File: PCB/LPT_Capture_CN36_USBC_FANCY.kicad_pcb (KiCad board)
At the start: 2 copper layers, 68 x 31.7 mm, 26 parts, among them J1 GSB1C411101DS1HR, J2 112-036-213R001, Q1 SL2301S, Q2 SL2301S, U1 FT245RL

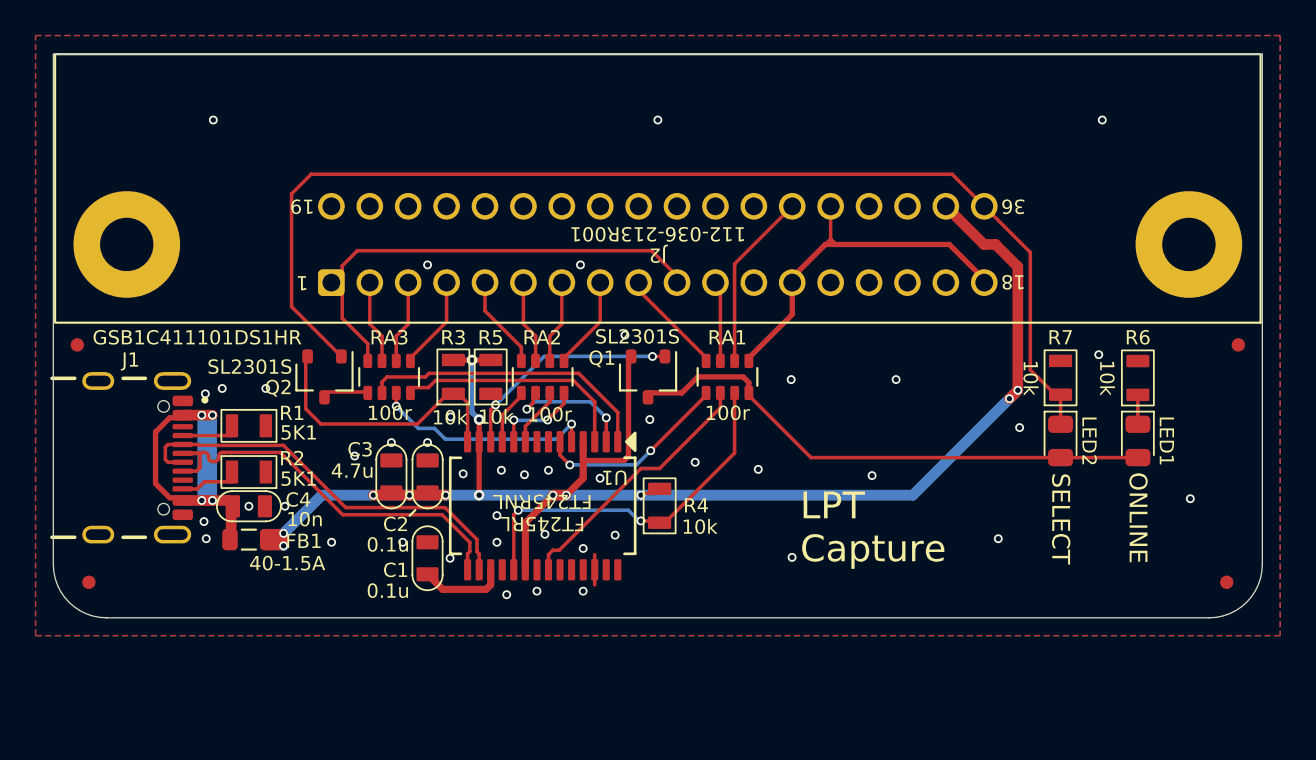
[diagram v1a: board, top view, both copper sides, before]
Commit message: cn36: board dims, leds, housing
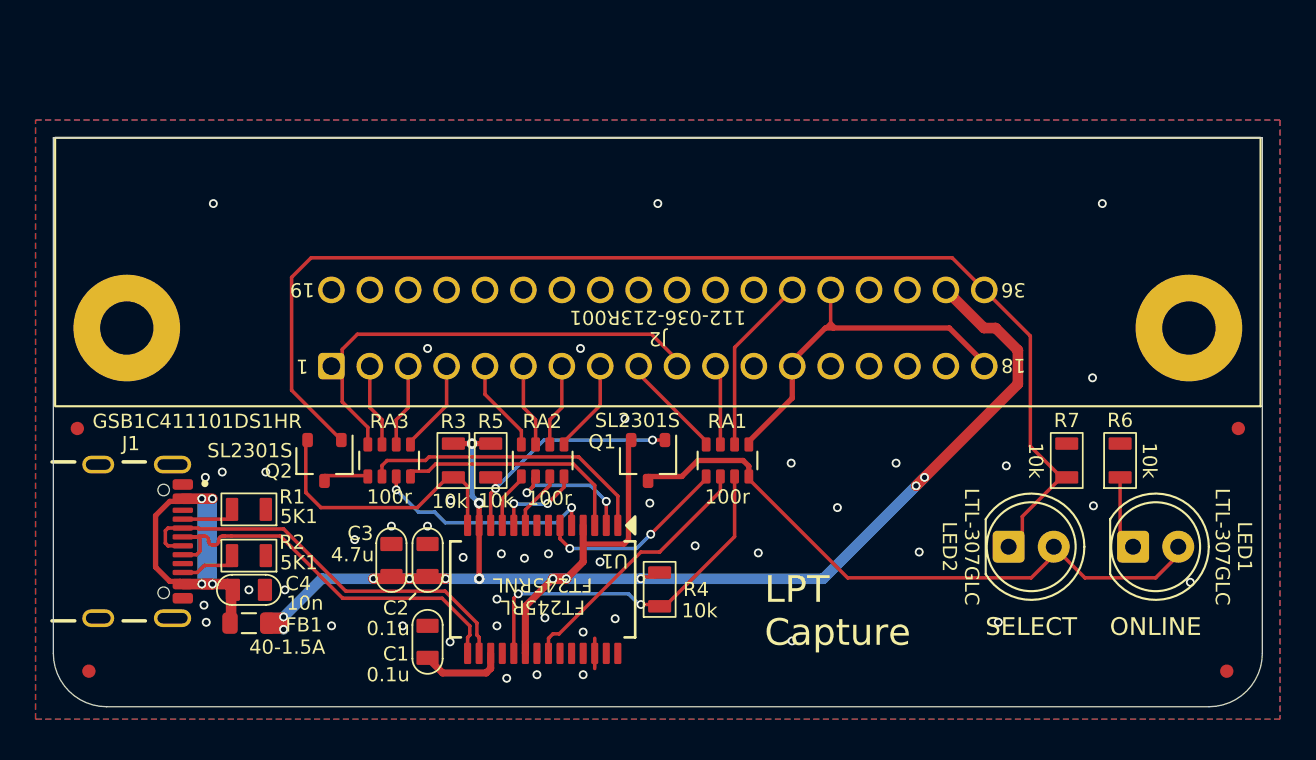
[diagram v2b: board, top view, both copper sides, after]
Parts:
- added N1: Housing, 000_LOCAL:Housing_CN36_shell_snap, F.Cu at (150.0, 100.0)
- LED1: value ONLINE -> LTL-307GLC; footprint 000_LOCAL:LED_0805 -> 000_LOCAL:LED_D5.0mm
- LED2: value SELECT -> LTL-307GLC; footprint 000_LOCAL:LED_0805 -> 000_LOCAL:LED_D5.0mm
- moved LED2 6.17 mm to (171.0, 107.0), turned to 0 degrees
- moved LED1 6.03 mm to (178.0, 107.0), turned to 0 degrees
- moved REF** 5.00 mm to (118.0, 114.0)
- moved REF** 5.00 mm to (182.0, 114.0)
- moved R6 4.75 mm to (176.0, 102.2)
- moved C2 4.70 mm to (137.1, 107.7)
- moved C3 4.70 mm to (135.0, 107.7)
- moved C4 4.70 mm to (127.0, 109.4)
- moved FB1 4.70 mm to (127.0, 111.3)
- moved J1 4.70 mm to (118.5, 106.7)
- moved J2 4.70 mm to (150.0, 94.7)
- moved Q1 4.70 mm to (149.4, 102.2)
- moved Q2 4.70 mm to (131.2, 102.2)
- moved R1 4.70 mm to (127.0, 104.9)
- moved R2 4.70 mm to (127.0, 107.5)
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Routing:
- net /ONLINE: track 30.5 -> 36.3 mm
- net /~{SELIN}: track 64.9 -> 68.7 mm
- net VCC: track 90.8 -> 87.9 mm
- net Net-(LED1-K): track 1.65 -> 4.20 mm
- net GND: vias 44 -> 46
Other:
- board size 68 x 31.7 mm -> 68 x 32 mm

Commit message: cn36 cover shape
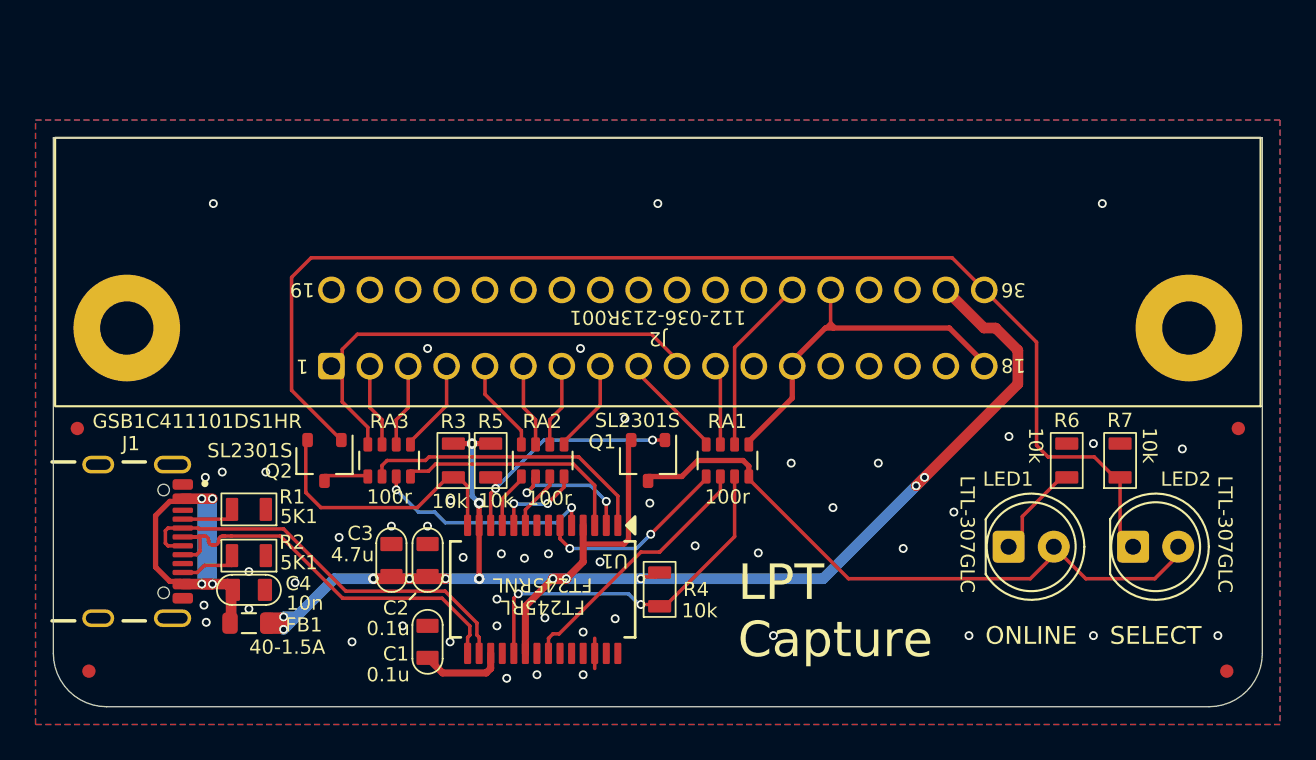
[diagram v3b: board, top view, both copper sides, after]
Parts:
- renumbered LED2 to LED1, LED1 to LED2, R7 to R6, R6 to R7
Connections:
- LED1 pad 1: /~{SELIN} -> Net-(LED1-K)
- LED2 pad 1: Net-(LED1-K) -> /~{SELIN}
- R6 pad 1: /~{SELIN} -> Net-(LED1-K)
- R7 pad 1: Net-(LED1-K) -> /~{SELIN}
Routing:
- net /~{SELIN}: track 68.7 -> 70.3 mm
- net Net-(LED1-K): track 4.20 -> 5.43 mm
- net GND: vias 46 -> 49

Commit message: cn36: missing datasheet, add RA4, refactor parts of cover scad
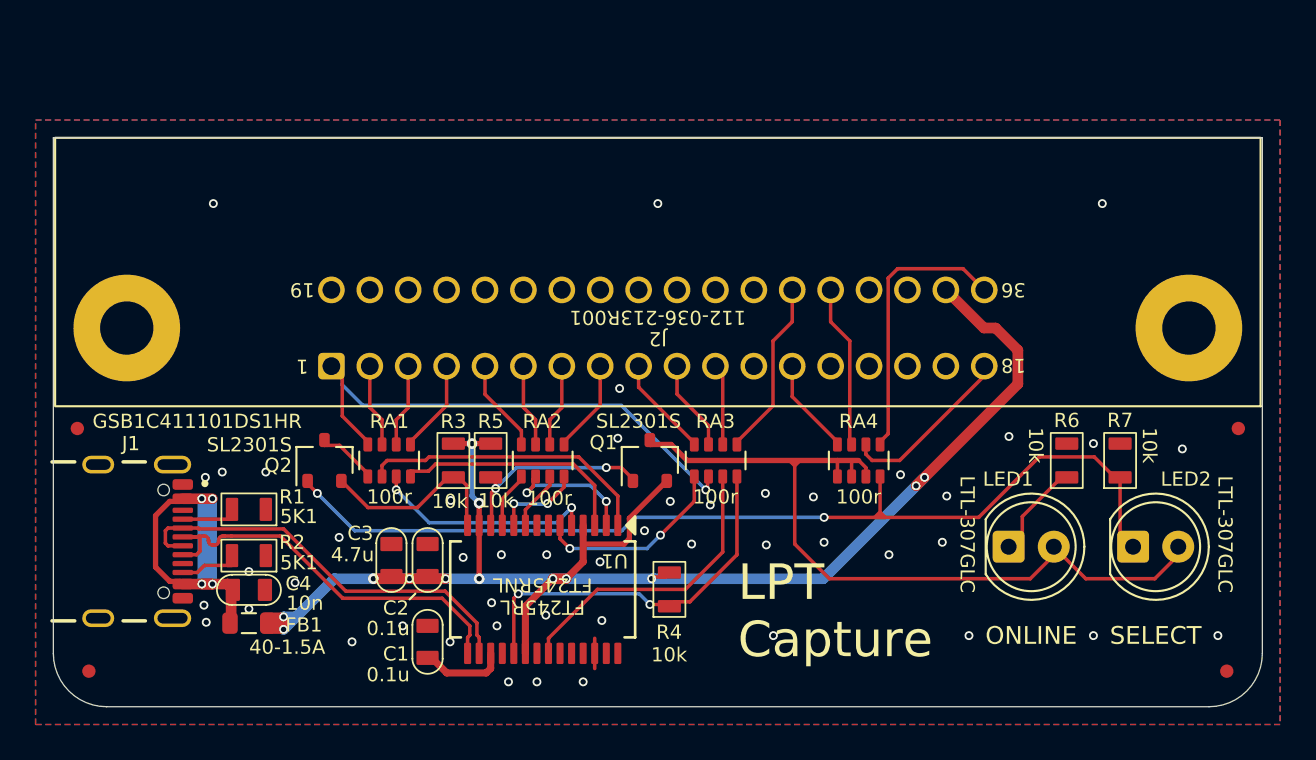
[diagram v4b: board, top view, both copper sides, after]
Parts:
- added RA4: 100r, 000_LOCAL:R_Array_Convex_4x0603, F.Cu at (161.3, 102.2)
- moved RA3 0.67 mm to (153.2, 102.2)
- moved R4 0.55 mm to (150.7, 109.4)
- moved Q1 0.10 mm to (149.6, 102.2), turned to 90 degrees
- turned Q2 to 90 degrees
- renumbered RA3 to RA1, RA1 to RA3
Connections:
- J2 pad 10: /~{pSTROBE} -> /~{ACK}
- J2 pad 18: /pONLINE -> /PLH
- J2 pad 32: /pONLINE -> /~{ERROR}
- J2 pad 36: /~{SELIN} -> /~{pSELIN}
- RA3 pad 2: /~{TXE} -> /~{pSTROBE}
- RA3 pad 3: /~{RESET} -> /~{TXE}
- RA3 pad 4: /ONLINE -> /~{RESET}
- RA3 pad 5: /pONLINE -> /~{pRESET}
- RA3 pad 6: /~{pRESET} -> /BUSY
- RA3 pad 7: /BUSY -> /~{ACK}
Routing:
- net /~{pSELIN}: track 0.00 -> 15.8 mm
- net /pONLINE: track 20.5 -> 5.46 mm
- net /~{SELIN}: track 70.3 -> 55.6 mm, vias 0 -> 2
- net /PLH: track 0.00 -> 9.87 mm
- net /~{ERROR}: track 0.00 -> 9.18 mm
- net /ONLINE: track 36.4 -> 45.1 mm
- net /~{ACK}: track 0.00 -> 5.14 mm
- net /WR: track 15.6 -> 10.8 mm
- net /~{pSTROBE}: track 26.6 -> 30.3 mm, vias 0 -> 1
- net /~{TXE}: track 14.8 -> 16.9 mm
- net /~{PWREN}: track 13.7 -> 11.7 mm
- net VCC: track 87.9 -> 86.4 mm
- net /~{STROBE}: track 2.76 -> 3.56 mm
- net /~{RESET}: track 20.9 -> 21.6 mm
- net GND: vias 49 -> 48

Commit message: cn36 add F1 SW1
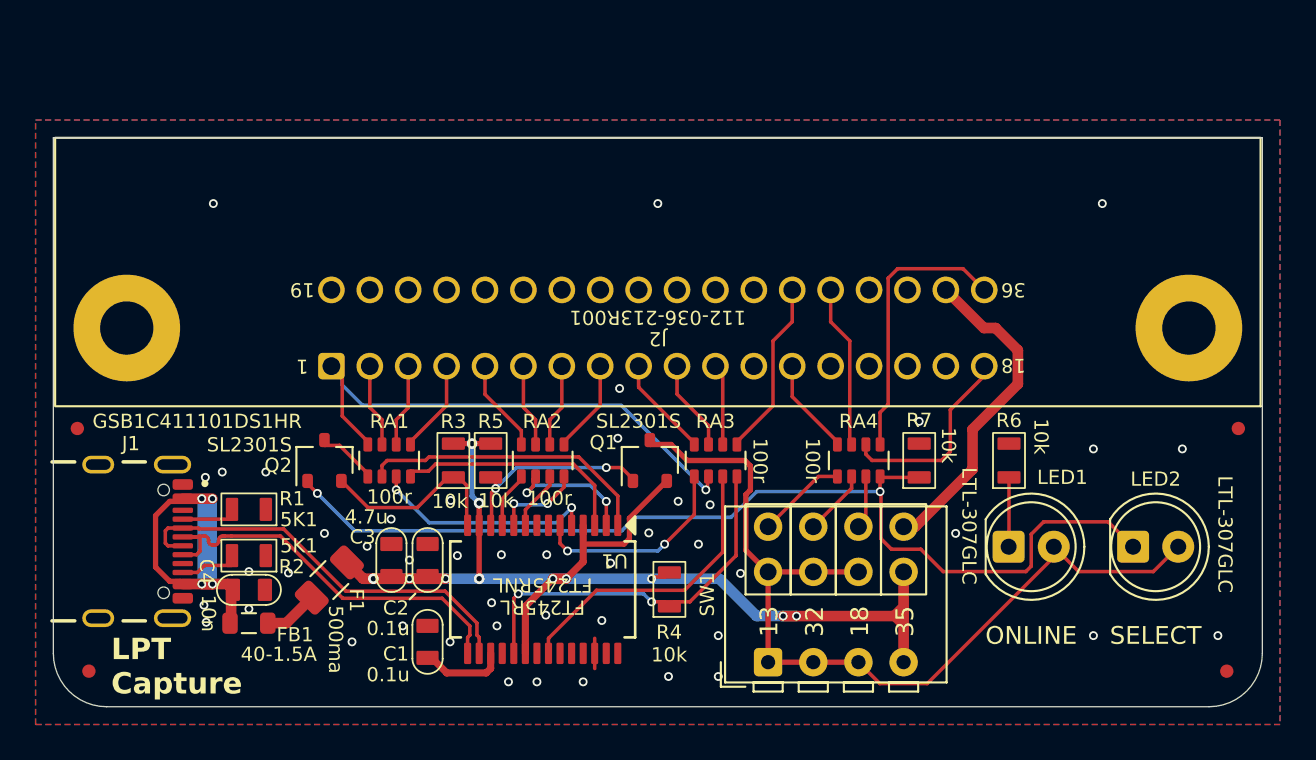
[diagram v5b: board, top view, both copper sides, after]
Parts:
- added F1: 500ma, 000_LOCAL:F_1206, F.Cu at (131.5, 108.9)
- added SW1: SW_DIP_x04, 000_LOCAL:SW_DIP_SPSTx04_Piano_Jumper_dual, F.Cu at (160.0, 109.7)
- moved R7 11.3 mm to (164.7, 102.2)
- moved R6 3.25 mm to (169.8, 102.2)
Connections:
- net /pD0 renamed /PD0
- net /pD1 renamed /PD1
- net /pD2 renamed /PD2
- net /pD3 renamed /PD3
- net /pD4 renamed /PD4
- net /pD5 renamed /PD5
- net /pD6 renamed /PD6
- net /pD7 renamed /PD7
- net /~{pRESET} renamed /~{INIT}
- FB1 pad 2: VCC -> Net-(F1-Pad1)
- J2 pad 1: /~{pSTROBE} -> /~{STROBE}
- J2 pad 13: /pONLINE -> /ONLINE
- J2 pad 35: VCC -> /5V
- J2 pad 36: /~{pSELIN} -> /~{SELIN}
- LED1 pad 2: /ONLINE -> /ON
- LED2 pad 1: /~{SELIN} -> /~{SEL}
- LED2 pad 2: /ONLINE -> /ON
- Q1 pad 3: /ONLINE -> /ON
- Q2 pad 1: /~{SELIN} -> /~{SEL}
- Q2 pad 3: /~{STROBE} -> /~{STR}
- R7 pad 1: /~{SELIN} -> /~{SEL}
- RA1 pad 1: /~{STROBE} -> /~{STR}
- RA1 pad 8: /~{pSTROBE} -> /~{STROBE}
- RA3 pad 2: /~{pSTROBE} -> /~{STROBE}
- RA4 pad 1: /ONLINE -> /sONL
- RA4 pad 2: /ONLINE -> /sERR
- RA4 pad 3: /ONLINE -> /sPLH
- RA4 pad 4: /~{SELIN} -> /~{SEL}
- RA4 pad 5: /~{pSELIN} -> /~{SELIN}
- RA4 pad 8: /pONLINE -> /ONLINE
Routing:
- net /~{SEL}: track 0.00 -> 57.8 mm, vias 0 -> 2
- net /ON: track 0.00 -> 51.4 mm
- net /~{SELIN}: track 55.6 -> 15.8 mm, vias 2 -> 0
- net /ONLINE: track 45.1 -> 5.46 mm
- net /~{pSTROBE}: track 30.3 -> 0.00 mm, vias 1 -> 0
- net /~{STROBE}: track 3.56 -> 30.3 mm, vias 0 -> 1
- net /5V: track 0.00 -> 18.4 mm
- net VCC: track 86.4 -> 69.3 mm, vias 13 -> 11
- net /~{pSELIN}: track 15.8 -> 0.00 mm
- net /pONLINE: track 5.46 -> 0.00 mm
- net /sONL: track 0.00 -> 5.07 mm
- net /sERR: track 0.00 -> 3.72 mm
- net /~{STR}: track 0.00 -> 3.56 mm
- net Net-(F1-Pad1): track 0.00 -> 3.07 mm
- net /sPLH: track 0.00 -> 3.00 mm
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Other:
- board text added: "13"
- board text added: "18"
- board text added: "32"
- board text added: "35"
- board text added: "ONLINE"
- board text added: "P13_ONL"
- board text added: "P18_PLH"
- board text added: "P32_~{ERR}"
- board text added: "P35_5V"
- board text added: "SELECT"
- board text added: "SW1 1: pin 13 ONLINE 2: pin 32 ~{ERROR} 3: pin 18 Peripheral Logic High 4: pin 35 5V Power"

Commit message: cn36 add jp1,2,3
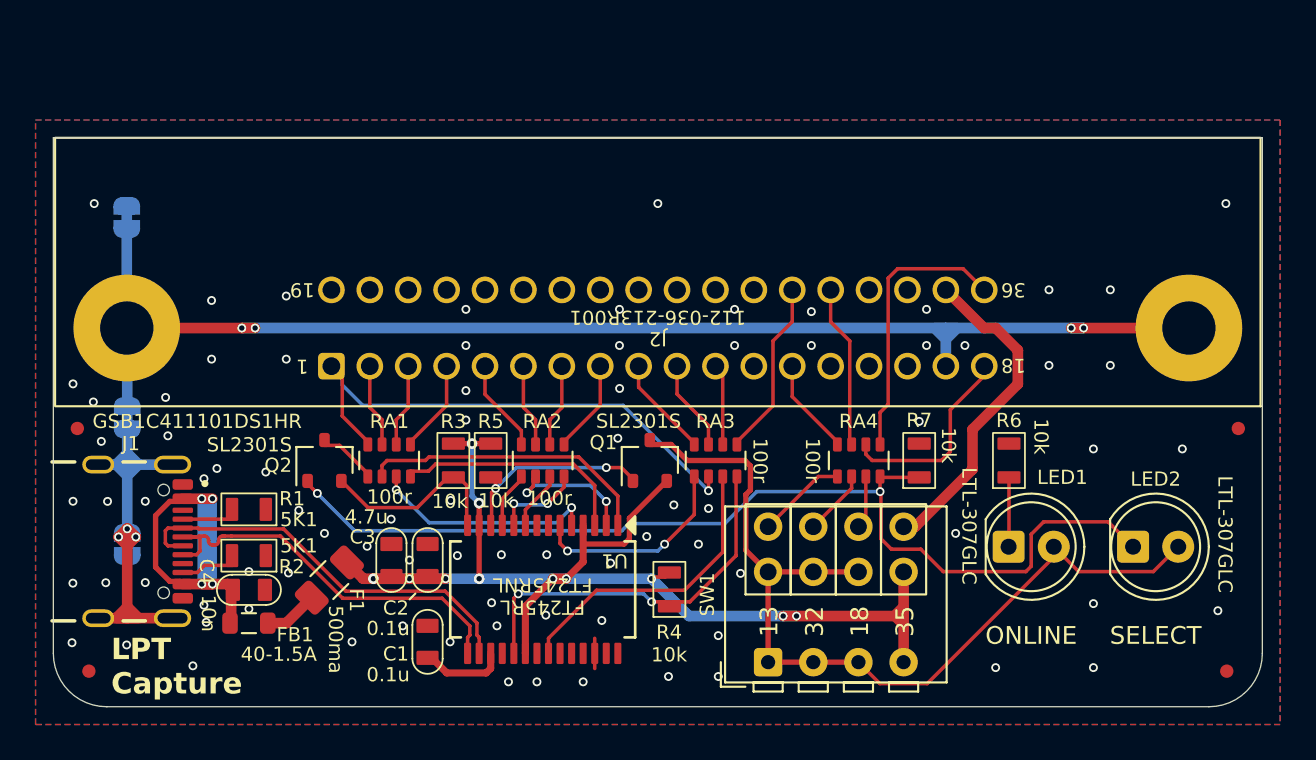
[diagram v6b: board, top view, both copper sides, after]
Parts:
- added JP1: GND_USBSHLD, 000_LOCAL:SolderJumper-2_P1.3mm_Bridged_RoundedPad1.0x1.5mm, B.Cu at (120.2, 106.9)
- added JP2: GND_LPTSHLD, 000_LOCAL:SolderJumper-2_P1.3mm_Bridged_RoundedPad1.0x1.5mm, B.Cu at (120.1, 88.5)
- added JP3: USBSHLD_LPTSHLD, 000_LOCAL:SolderJumper-2_P1.3mm_Bridged_RoundedPad1.0x1.5mm, B.Cu at (120.2, 99.7)
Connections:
- J1 pad S: GND -> USB_SHIELD
- J2 pad 17: GND -> LPT_SHIELD
- J2 pad S: GND -> LPT_SHIELD
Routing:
- net LPT_SHIELD: track 0.00 -> 74.0 mm, vias 0 -> 4
- net USB_SHIELD: track 0.00 -> 22.0 mm, vias 0 -> 3
- net GND: vias 46 -> 84
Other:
- board text added: "GND LPT SHIELD"
- board text added: "LPT SHIELD USB SHIELD"
- board text added: "USB SHIELD GND"

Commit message: cn36 add R8 current limit led when /SELIN driven low
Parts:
- added R8: 10k, 000_LOCAL:R_0805, F.Cu at (175.2, 102.2)
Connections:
- LED2 pad 1: /~{SEL} -> Net-(LED2-K)
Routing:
- net Net-(LED2-K): track 0.00 -> 4.71 mm
